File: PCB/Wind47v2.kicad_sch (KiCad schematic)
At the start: 144 parts, among them SW1 RotaryEncoder_Switch, SW2 RotaryEncoder_Switch, U2 RP2040_Pro_Micro

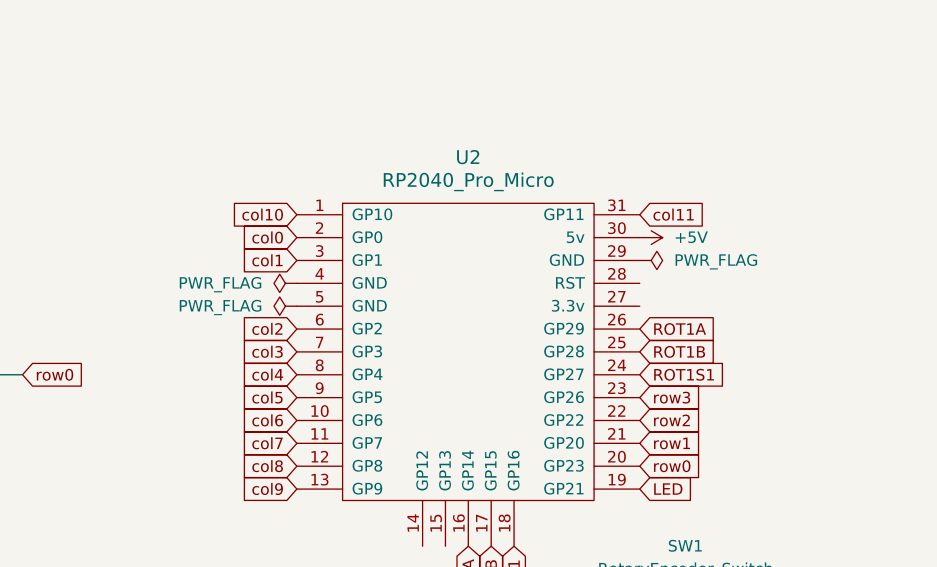
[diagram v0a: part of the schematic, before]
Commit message: Update PCB net assignments and production files
Renamed and reordered several net assignments in Wind47v2.kicad_pcb to remove unused nets and improve clarity. Updated production STL and ZIP files, removed outdated backups, and added new 3D and PCB files. Journal updated with design changes for USB-C port and floor thickness adjustment.
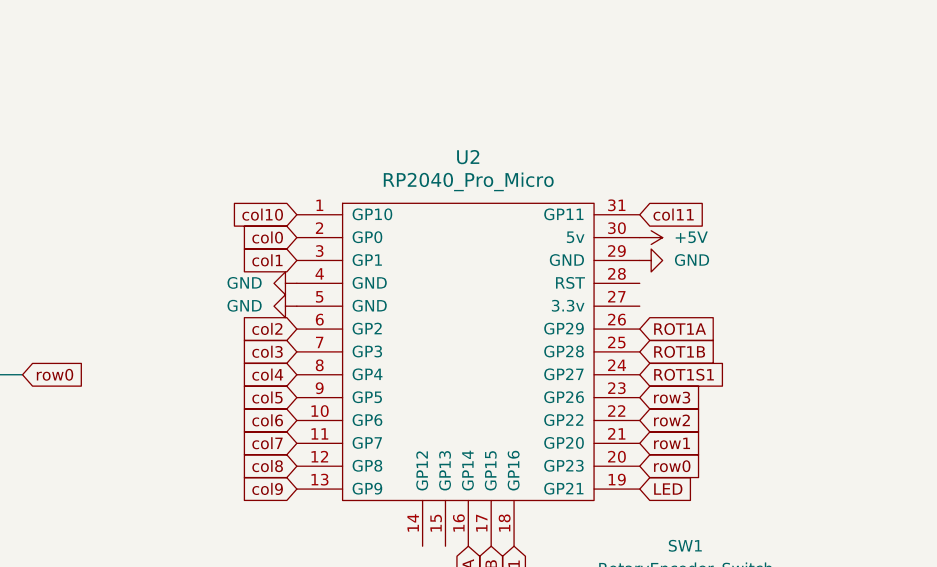
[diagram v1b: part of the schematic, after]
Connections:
- net GND: now also U2.29 (GND), U2.4 (GND), U2.5 (GND)
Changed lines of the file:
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@@
 	)
 	(symbol
+		(lib_id "power:GND")
+		(at 273.05 38.1 90)
+		(unit 1)
+		(exclude_from_sim no)
+		(in_bom yes)
+		(on_board yes)
+		(dnp no)
+		(fields_autoplaced yes)
+		(property "Reference" "#PWR10"
+			(at 279.4 38.1 0)
+			(effects
+				(font
+					(size 1.27 1.27)
+				)
+				(hide yes)
+			)
+		)
+		(property "Value" "GND"
+			(at 276.86 38.0999 90)
+			(effects
+				(font
+					(size 1.27 1.27)
+				)
+				(justify right)
+			)
+		)
+		(property "Footprint" ""
+			(at 273.05 38.1 0)
+			(effects
+				(font
+					(size 1.27 1.27)
+				)
+				(hide yes)
+			)
+		)
+		(property "Datasheet" ""
+			(at 273.05 38.1 0)
+			(effects
+				(font
+					(size 1.27 1.27)
+				)
+				(hide yes)
+			)
+		)
+		(property "Description" "Power symbol creates a global label with name \"GND\" , ground"
+			(at 273.05 38.1 0)
+			(effects
+				(font
+					(size 1.27 1.27)
+				)
+				(hide yes)
+			)
+		)
+		(pin "1"
+		)
+		(instances
+			(project "Wind47v2"
+				(path "/3221dfaf-3c2d-48a5-8e34-90019b82225a"
+					(reference "#PWR10")
+					(unit 1)
+				)
+			)
+		)
+	)
+	(symbol
 		(lib_id "ScottoKeebs:Placeholder_Keyswitch")
 		(at 93.98 66.04 0)
@@
 	)
 	(symbol
-		(lib_id "power:PWR_FLAG")
-		(at 273.05 38.1 270)
+		(lib_id "ScottoKeebs:LED_SK6812MINI")
+		(at 414.02 20.32 0)
 		(unit 1)
 		(exclude_from_sim no)
@@
 		(dnp no)
 		(fields_autoplaced yes)
-		(property "Reference" "#FLG3"
-			(at 274.955 38.1 0)
-			(effects
-				(font
-					(size 1.27 1.27)
-				)
-				(hide yes)
-			)
-		)
-		(property "Value" "PWR_FLAG"
-			(at 276.86 38.0999 90)
+		(property "Reference" "D53"
+			(at 427.99 11.4614 0)
 			(effects
 				(font
 					(size 1.27 1.27)
 				)
-				(justify left)
 			)
 		)
-		(property "Footprint" ""
-			(at 273.05 38.1 0)
+		(property "Value" "LED_SK6812MINI"
+			(at 427.99 14.0014 0)
 			(effects
 				(font
 					(size 1.27 1.27)
 				)
-				(hide yes)
 			)
 		)
-		(property "Datasheet" "~"
-			(at 273.05 38.1 0)
+		(property "Footprint" "ScottoKeebs_Components:LED_SK6812MINI"
+			(at 415.29 27.94 0)
 			(effects
 				(font
 					(size 1.27 1.27)
 				)
+				(justify left top)
 				(hide yes)
 			)
 		)
-		(property "Description" "Special symbol for telling ERC where power comes from"
-			(at 273.05 38.1 0)
+		(property "Datasheet" "https://cdn-shop.adafruit.com/product-files/2686/SK6812MINI_REV.01-1-2.pdf"
+			(at 415.29 31.496 0)
 			(effects
 				(font
 					(size 1.27 1.27)
 				)
+				(justify left top)
 				(hide yes)
 			)
 		)
-		(pin "1"
-		)
-		(instances
-			(project ""
-				(path "/3221dfaf-3c2d-48a5-8e34-90019b82225a"
-					(reference "#FLG3")
-					(unit 1)
-				)
-			)
-		)
-	)
-	(symbol
-		(lib_id "power:PWR_FLAG")
-		(at 234.95 40.64 90)
-		(unit 1)
-		(exclude_from_sim no)
-		(in_bom yes)
-		(on_board yes)
-		(dnp no)
-		(fields_autoplaced yes)
-		(property "Reference" "#FLG1"
-			(at 233.045 40.64 0)
+		(property "Description" "RGB LED with integrated controller"
+			(at 432.308 30.48 0)
 			(effects
 				(font
@@
 			)
 		)
-		(property "Value" "PWR_FLAG"
-			(at 231.14 40.6399 90)
-			(effects
-				(font
-					(size 1.27 1.27)
-				)
-				(justify left)
-			)
-		)
-		(property "Footprint" ""
-			(at 234.95 40.64 0)
+		(property "LCSC" "C5149201"
+			(at 427.99 16.5414 0)
 			(effects
 				(font
 					(size 1.27 1.27)
 				)
-				(hide yes)
 			)
 		)
-		(property "Datasheet" "~"
-			(at 234.95 40.64 0)
-			(effects
-				(font
-					(size 1.27 1.27)
-				)
-				(hide yes)
-			)
+		(pin "3"
 		)
-		(property "Description" "Special symbol for telling ERC where power comes from"
-			(at 234.95 40.64 0)
-			(effects
-				(font
-					(size 1.27 1.27)
-				)
-				(hide yes)
-			)
+		(pin "2"
 		)
 		(pin "1"
 		)
+		(pin "4"
+		)
 		(instances
-			(project ""
+			(project "SolarKey"
 				(path "/3221dfaf-3c2d-48a5-8e34-90019b82225a"
-					(reference "#FLG1")
+					(reference "D53")
 					(unit 1)
 				)
@@
 	)
 	(symbol
-		(lib_id "ScottoKeebs:LED_SK6812MINI")
-		(at 414.02 20.32 0)
+		(lib_id "power:GND")
+		(at 234.95 40.64 270)
 		(unit 1)
 		(exclude_from_sim no)
@@
 		(dnp no)
 		(fields_autoplaced yes)
-		(property "Reference" "D53"
-			(at 427.99 11.4614 0)
+		(property "Reference" "#PWR8"
+			(at 228.6 40.64 0)
 			(effects
 				(font
 					(size 1.27 1.27)
 				)
+				(hide yes)
 			)
 		)
-		(property "Value" "LED_SK6812MINI"
-			(at 427.99 14.0014 0)
+		(property "Value" "GND"
+			(at 231.14 40.6399 90)
 			(effects
 				(font
 					(size 1.27 1.27)
 				)
+				(justify right)
 			)
 		)
-		(property "Footprint" "ScottoKeebs_Components:LED_SK6812MINI"
-			(at 415.29 27.94 0)
+		(property "Footprint" ""
+			(at 234.95 40.64 0)
 			(effects
 				(font
 					(size 1.27 1.27)
 				)
-				(justify left top)
 				(hide yes)
 			)
 		)
-		(property "Datasheet" "https://cdn-shop.adafruit.com/product-files/2686/SK6812MINI_REV.01-1-2.pdf"
-			(at 415.29 31.496 0)
+		(property "Datasheet" ""
+			(at 234.95 40.64 0)
 			(effects
 				(font
 					(size 1.27 1.27)
 				)
-				(justify left top)
 				(hide yes)
 			)
 		)
-		(property "Description" "RGB LED with integrated controller"
-			(at 432.308 30.48 0)
+		(property "Description" "Power symbol creates a global label with name \"GND\" , ground"
+			(at 234.95 40.64 0)
 			(effects
 				(font
@@
 			)
 		)
-		(property "LCSC" "C5149201"
-			(at 427.99 16.5414 0)
-			(effects
-				(font
-					(size 1.27 1.27)
-				)
-			)
-		)
-		(pin "3"
-		)
-		(pin "2"
-		)
 		(pin "1"
 		)
-		(pin "4"
-		)
 		(instances
-			(project "SolarKey"
+			(project ""
 				(path "/3221dfaf-3c2d-48a5-8e34-90019b82225a"
-					(reference "D53")
+					(reference "#PWR8")
 					(unit 1)
 				)
@@
 	)
 	(symbol
-		(lib_id "power:PWR_FLAG")
-		(at 234.95 43.18 90)
+		(lib_id "power:GND")
+		(at 234.95 43.18 270)
 		(unit 1)
 		(exclude_from_sim no)
@@
 		(dnp no)
 		(fields_autoplaced yes)
-		(property "Reference" "#FLG2"
-			(at 233.045 43.18 0)
+		(property "Reference" "#PWR9"
+			(at 228.6 43.18 0)
 			(effects
 				(font
@@
 			)
 		)
-		(property "Value" "PWR_FLAG"
+		(property "Value" "GND"
 			(at 231.14 43.1799 90)
 			(effects
@@
 					(size 1.27 1.27)
 				)
-				(justify left)
+				(justify right)
 			)
 		)
@@
 			)
 		)
-		(property "Datasheet" "~"
+		(property "Datasheet" ""
 			(at 234.95 43.18 0)
 			(effects
@@
 			)
 		)
-		(property "Description" "Special symbol for telling ERC where power comes from"
+		(property "Description" "Power symbol creates a global label with name \"GND\" , ground"
 			(at 234.95 43.18 0)
 			(effects
@@
 		)
 		(instances
-			(project ""
+			(project "Wind47v2"
 				(path "/3221dfaf-3c2d-48a5-8e34-90019b82225a"
-					(reference "#FLG2")
+					(reference "#PWR9")
 					(unit 1)
 				)
